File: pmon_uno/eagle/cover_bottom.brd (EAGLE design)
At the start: 56 x 56 mm, 0 parts

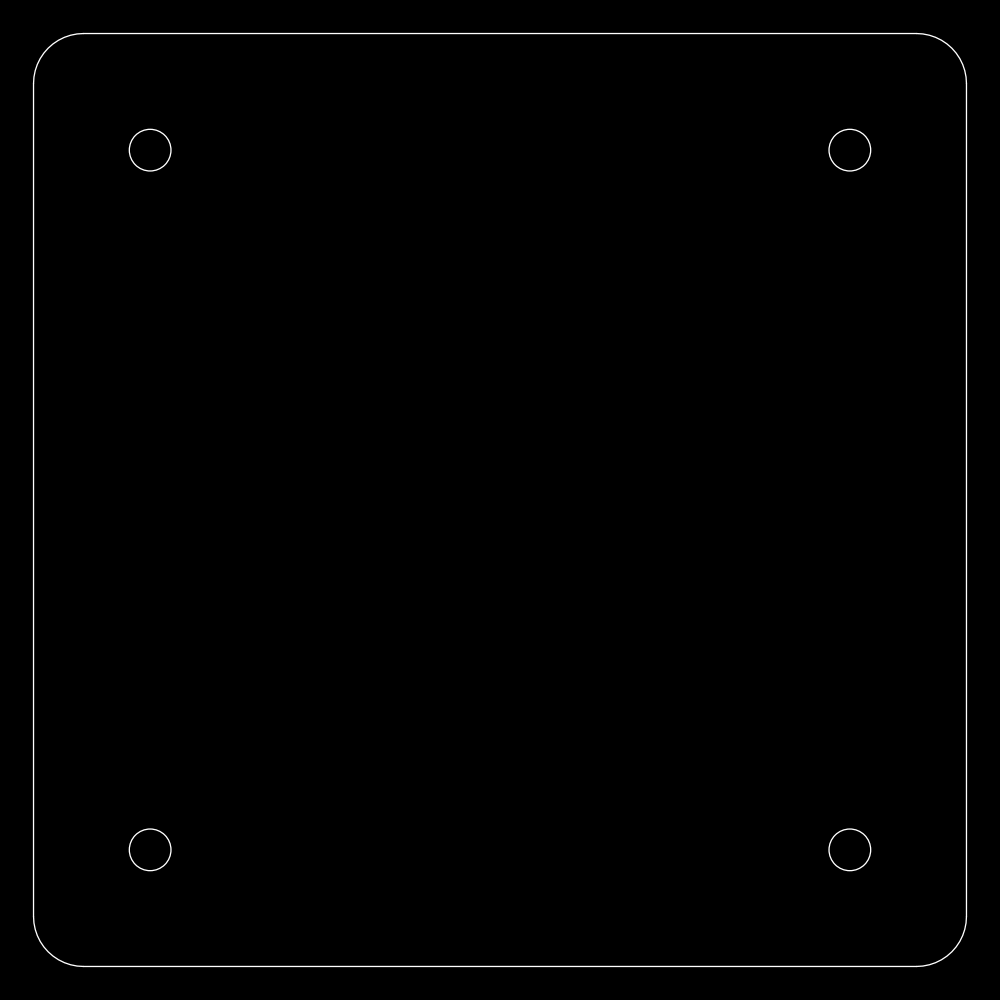
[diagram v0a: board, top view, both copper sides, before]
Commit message: Minor Eagle tweaks: 1. Added a debug pin to the logic analyzer signals. 2. Changed the top and bottom drill sizes from 2.5mm to 3mm.
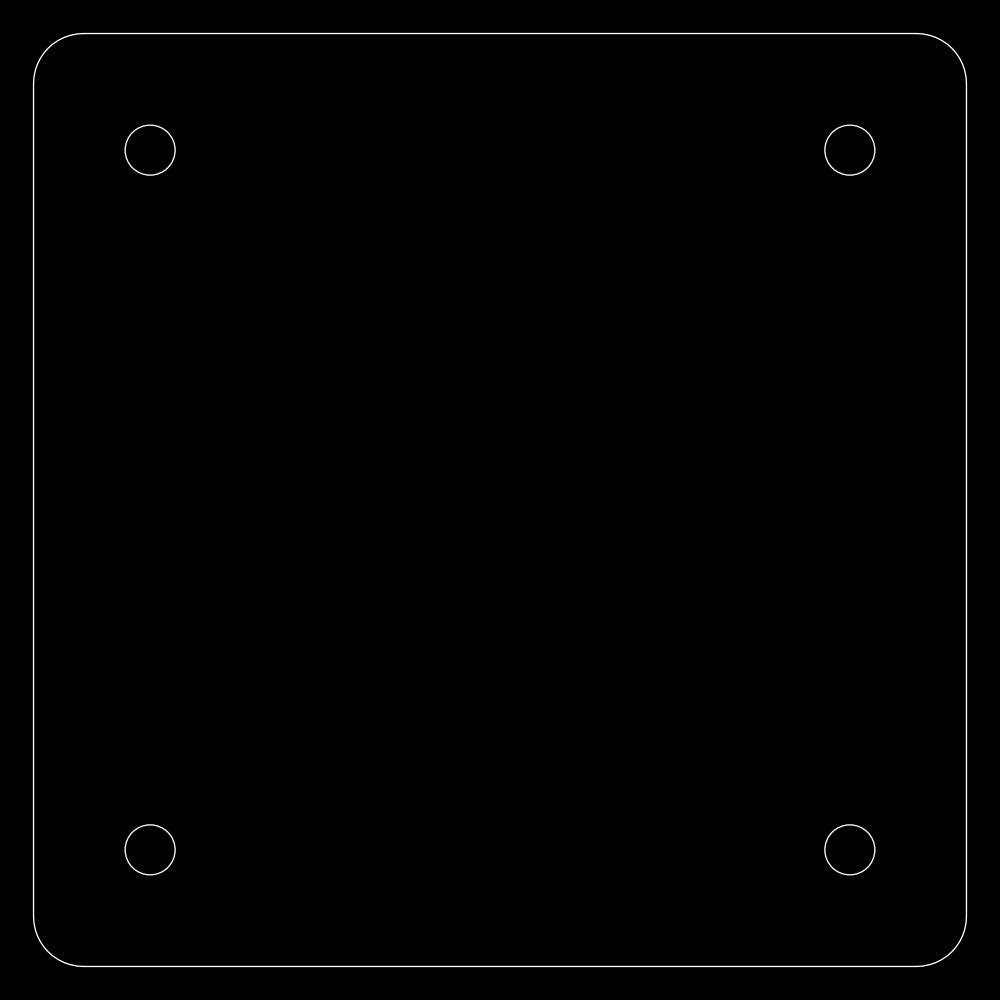
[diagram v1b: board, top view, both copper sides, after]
